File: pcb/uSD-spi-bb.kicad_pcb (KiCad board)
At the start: 2 copper layers, 36 x 36 mm, 25 parts, among them U1 TLV70233DBV, U2 MicroSD

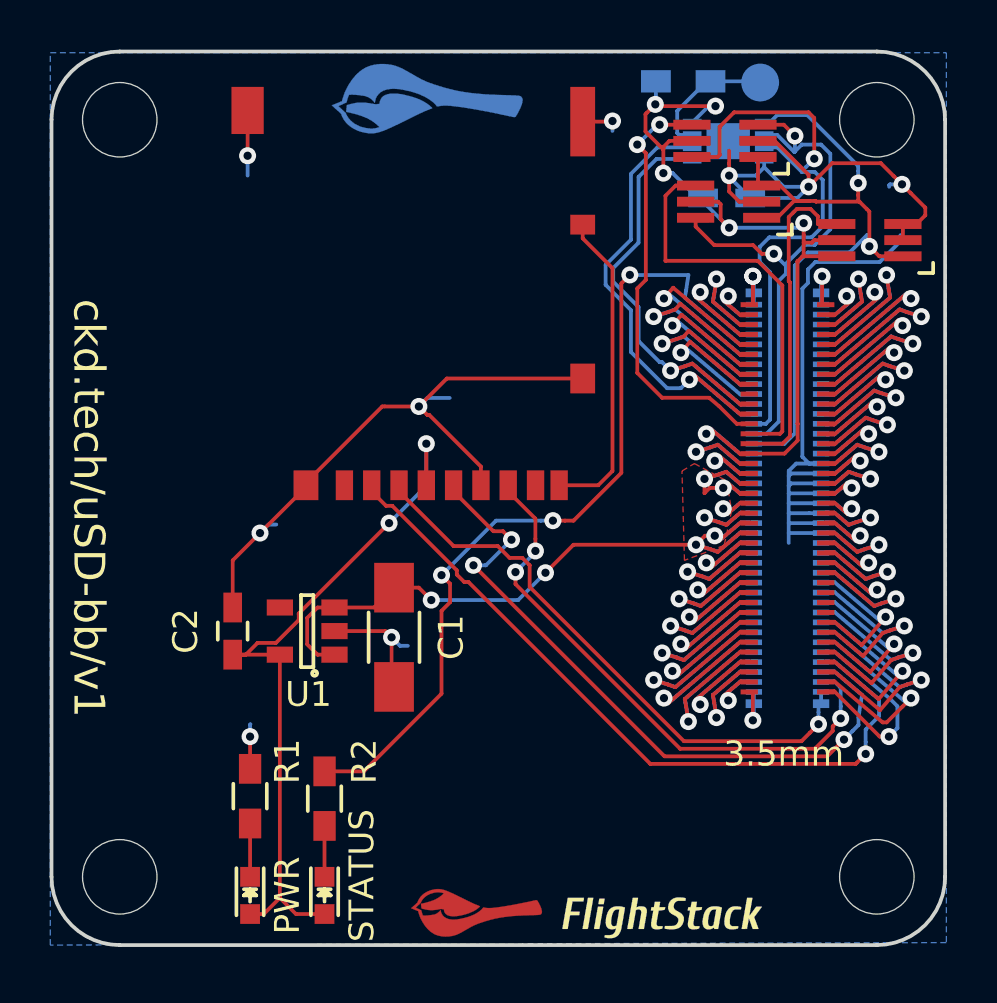
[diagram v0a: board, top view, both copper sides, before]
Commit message: Add card detect to uSD BB.
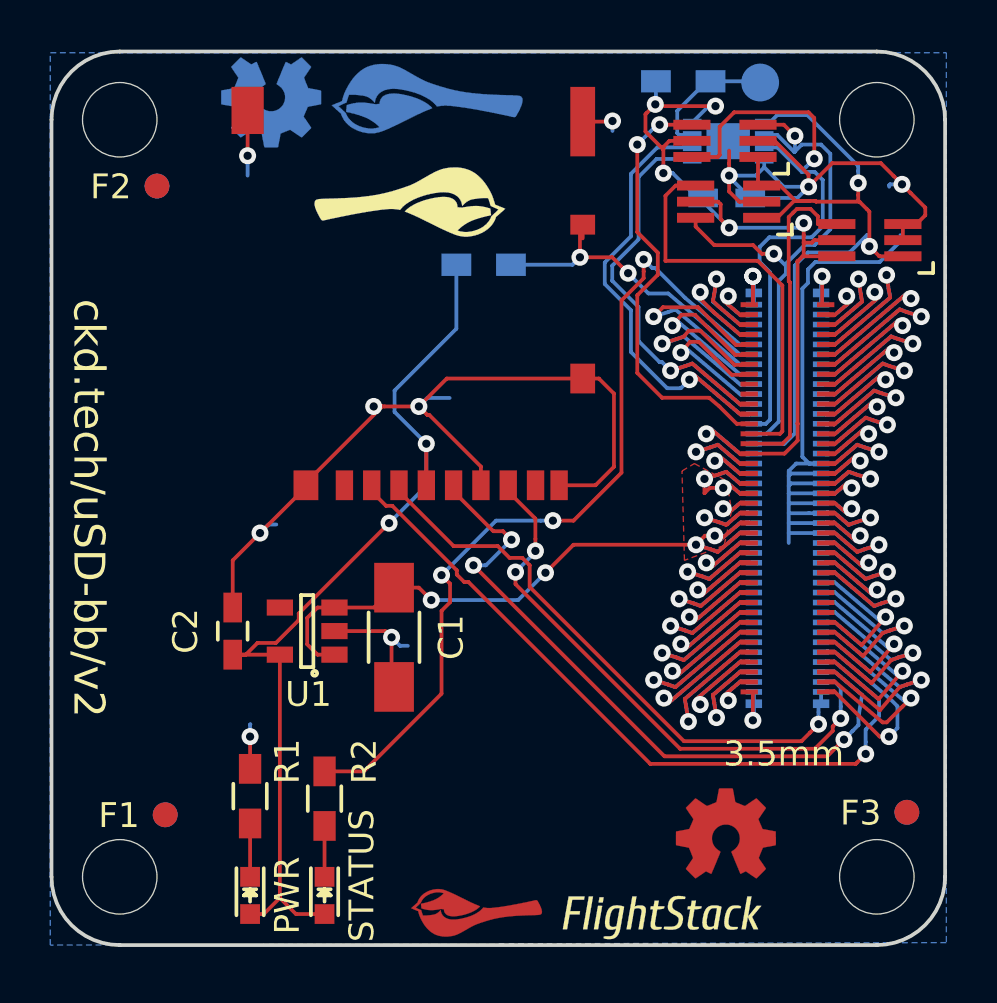
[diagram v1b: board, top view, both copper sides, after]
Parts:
- removed the G*** at (154.6, 124.9)
- removed the G*** at (131.5, 108.1)
- added F1: 1mm, macrofab:Fiducial, F.Cu at (134.6, 120.8)
- added F2: 1mm, macrofab:Fiducial, F.Cu at (134.2, 95.4)
- added F3: 1mm, macrofab:Fiducial, F.Cu at (164.5, 120.7)
- added F4: 1mm, macrofab:Fiducial, B.Cu at (134.6, 120.8)
- added F5: 1mm, macrofab:Fiducial, B.Cu at (134.2, 95.4)
- added F6: 1mm, macrofab:Fiducial, B.Cu at (164.5, 120.7)
- added G***: LOGO, flightstack:flightstack_thin-8mm, F.Cu at (154.6, 124.9)
- added G***: LOGO, flightstack:flightstack_thin-12mm, B.Cu at (131.5, 108.1)
- added G***: OSHW, oshw:oshw-4mm, B.Cu at (138.8, 92.0)
- added G***: OSHW, oshw:oshw-4mm, F.Cu at (157.2, 121.5)
- added G***: LOGO, chickadee:chickadee_3mm_ss, F.Cu at (144.3, 96.0)
- added R3: 10k, Resistors_SMD:R_0603_HandSoldering, B.Cu at (147.4, 98.6)
- U2: footprint microsd:DM3AT -> DM3AT
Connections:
- PORT_OUT1 pad 5: /ExpansionPort/GPIO2 -> /ExpansionPort/GPIO3
- PORT_OUT1 pad 6: /ExpansionPort/GPIO3 -> /ExpansionPort/GPIO4
- PORT_OUT1 pad 7: /ExpansionPort/GPIO4 -> /ExpansionPort/GPIO5
- PORT_OUT1 pad 8: /ExpansionPort/GPIO5 -> /ExpansionPort/GPIO6
- PORT_OUT1 pad 9: /ExpansionPort/GPIO6 -> Net-(PORT_OUT1-Pad9)
- U2 pad 9: Net-(U2-Pad9) -> GNDPWR
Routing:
- net Net-(U2-Pad9): track 12.8 -> 0.00 mm
- net +3V3: track 29.4 -> 38.2 mm
- net GNDPWR: track 116.0 -> 123.4 mm, vias 17 -> 18
- net /ExpansionPort/GPIO2: track 8.93 -> 13.2 mm, vias 1 -> 2
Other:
- board text added: "ckd.tech/uSD-bb/v2"
- board text removed: "ckd.tech/uSD-bb/v1"

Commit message: Rebrand everything to Polystack and increment versions.
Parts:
- removed the G*** at (154.6, 124.9)
- removed the G*** at (131.5, 108.1)
- added svg2mod: G***, polystack:polystack-medium-0.4, B.Cu at (164.9, 107.9)
- added svg2mod: G***, polystack:polystack-medium-0.4, F.Cu at (164.9, 107.9)
- added svg2mod: G***, polystack:polystack-medium-0.5, F.Cu at (154.8, 124.5)
- moved G*** 8.60 mm to (147.4, 92.2), turned to 180 degrees
- moved G*** 4.42 mm to (140.7, 92.3), turned to 180 degrees
- turned G*** to 0 degrees
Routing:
- net GNDPWR: track 123.4 -> 122.4 mm
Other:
- rule pad_to_mask_clearance: 0.2 -> 0.0762
- board text added: "ckd.tech/uSD-bb/v3"
- board text removed: "ckd.tech/uSD-bb/v2"

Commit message: Final gerbers for test manufacturing run.
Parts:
- moved U2 1.05 mm to (145.0, 99.8)
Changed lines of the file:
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@@
     (links 144)
     (no_connects 0)
-    (area 129.924999 89.924999 166.075001 126.075001)
+    (area 118.127143 74.1 234.166668 178)
     (thickness 1.6)
     (drawings 30)
@@
     (visible_elements FFFFFF7F)
     (pcbplotparams
-      (layerselection 0x010f0_80000001)
+      (layerselection 0x010fc_80000001)
       (usegerberextensions true)
       (excludeedgelayer true)
@@
     (add_net "Net-(U2-Pad1)")
     (add_net "Net-(U2-Pad8)")
+  )
+  (module DM3AT (layer F.Cu)
+    (at 145 99.75 180)
+    (fp_text reference U2 (at 0 1.55 180) (layer F.SilkS) hide
+      (effects (font (size 1 1) (thickness 0.15)))
+    )
+    (fp_text value MicroSD (at 0 0.55 360) (layer F.Fab)
+      (effects (font (size 1 1) (thickness 0.15)))
+    )
+    (fp_line (start -7.11 -4.35) (end -5.51 -4.41) (layer F.CrtYd) (width 0.15))
+    (fp_line (start -7.16 -6.66) (end -7.11 -4.35) (layer F.CrtYd) (width 0.15))
+    (fp_line (start -5.68 -6.6) (end -7.16 -6.66) (layer F.CrtYd) (width 0.15))
+    (fp_line (start -5.57 -4.53) (end -5.68 -6.6) (layer F.CrtYd) (width 0.15))
+    (fp_line (start -7.11 0.39) (end -7.05 -2.51) (layer F.CrtYd) (width 0.15))
+    (fp_line (start -5.63 0.39) (end -7.11 0.39) (layer F.CrtYd) (width 0.15))
+    (fp_line (start -5.63 -2.51) (end -5.63 0.39) (layer F.CrtYd) (width 0.15))
+    (fp_line (start -6.99 -2.51) (end -5.63 -2.51) (layer F.CrtYd) (width 0.15))
+    (fp_line (start -4.62 -0.92) (end -4.56 -2.63) (layer F.CrtYd) (width 0.15))
+    (fp_line (start 3.73 -0.86) (end -4.62 -0.92) (layer F.CrtYd) (width 0.15))
+    (fp_line (start 3.73 -2.63) (end 3.73 -0.86) (layer F.CrtYd) (width 0.15))
+    (fp_line (start -4.44 -2.63) (end 3.73 -2.63) (layer F.CrtYd) (width 0.15))
+    (fp_line (start -4.56 7.49) (end -5.57 7.55) (layer F.CrtYd) (width 0.15))
+    (fp_line (start -4.62 -0.44) (end -4.56 7.49) (layer F.CrtYd) (width 0.15))
+    (fp_line (start -5.45 -0.44) (end -4.62 -0.44) (layer F.CrtYd) (width 0.15))
+    (fp_line (start -5.51 7.55) (end -5.45 -0.44) (layer F.CrtYd) (width 0.15))
+    (fp_line (start 4.12 7.45) (end 5.5 7.45) (layer F.CrtYd) (width 0.15))
+    (fp_line (start 4.16 8.36) (end 4.12 7.45) (layer F.CrtYd) (width 0.15))
+    (fp_line (start 5.5 8.4) (end 4.16 8.36) (layer F.CrtYd) (width 0.15))
+    (fp_line (start 5.5 7.45) (end 5.5 8.4) (layer F.CrtYd) (width 0.15))
+    (fp_line (start -5.5 9.825) (end 5.5 9.825) (layer F.Fab) (width 0.15))
+    (pad 1 smd rect (at 3.2 -7.725 180) (size 0.7 1.2) (layers F.Cu F.Paste F.Mask)
+      (net 81 "Net-(U2-Pad1)"))
+    (pad 2 smd rect (at 2.1 -7.725 180) (size 0.7 1.2) (layers F.Cu F.Paste F.Mask)
+      (net 22 /ExpansionPort/SPI1_NSS))
+    (pad 3 smd rect (at 1 -7.725 180) (size 0.7 1.2) (layers F.Cu F.Paste F.Mask)
+      (net 16 /ExpansionPort/SPI1_MOSI))
+    (pad 4 smd rect (at -0.1 -7.725 180) (size 0.7 1.2) (layers F.Cu F.Paste F.Mask)
+      (net 11 +3V3))
+    (pad 5 smd rect (at -1.2 -7.725 180) (size 0.7 1.2) (layers F.Cu F.Paste F.Mask)
+      (net 21 /ExpansionPort/SPI1_SCK))
+    (pad 6 smd rect (at -2.3 -7.725 180) (size 0.7 1.2) (layers F.Cu F.Paste F.Mask)
+      (net 2 GNDPWR))
+    (pad 7 smd rect (at -3.4 -7.725 180) (size 0.7 1.2) (layers F.Cu F.Paste F.Mask)
+      (net 20 /ExpansionPort/SPI1_MISO))
+    (pad 8 smd rect (at -4.5 -7.725 180) (size 0.7 1.2) (layers F.Cu F.Paste F.Mask)
+      (net 82 "Net-(U2-Pad8)"))
+    (pad 9 smd rect (at -5.45 -7.725 180) (size 0.7 1.2) (layers F.Cu F.Paste F.Mask)
+      (net 2 GNDPWR))
+    (pad 10 smd rect (at 4.75 -7.725 180) (size 1 1.2) (layers F.Cu F.Paste F.Mask)
+      (net 2 GNDPWR))
+    (pad 11 smd rect (at 7.1 7.375 180) (size 1.3 1.9) (layers F.Cu F.Paste F.Mask)
+      (net 2 GNDPWR))
+    (pad 12 smd rect (at -6.4 6.925 180) (size 1 2.8) (layers F.Cu F.Paste F.Mask)
+      (net 2 GNDPWR))
+    (pad 14 smd rect (at -6.4 2.775 180) (size 1 0.8) (layers F.Cu F.Paste F.Mask)
+      (net 54 /ExpansionPort/GPIO2))
+    (pad 13 smd rect (at -6.4 -3.425 180) (size 1 1.2) (layers F.Cu F.Paste F.Mask)
+      (net 2 GNDPWR))
   )
   (module polystack:polystack-medium-0.4 (layer B.Cu)
@@
       (solder_mask_margin 0.5) (solder_paste_margin_ratio -0.5) (clearance 0.5))
   )
-  (module DM3AT (layer F.Cu)
-    (at 145 98.7 180)
-    (fp_text reference U2 (at 0 0.5 180) (layer F.SilkS) hide
-      (effects (font (size 1 1) (thickness 0.15)))
-    )
-    (fp_text value MicroSD (at 0 -0.5 360) (layer F.Fab)
-      (effects (font (size 1 1) (thickness 0.15)))
-    )
-    (fp_line (start -7.11 -5.4) (end -5.51 -5.46) (layer F.CrtYd) (width 0.15))
-    (fp_line (start -7.16 -7.71) (end -7.11 -5.4) (layer F.CrtYd) (width 0.15))
-    (fp_line (start -5.68 -7.65) (end -7.16 -7.71) (layer F.CrtYd) (width 0.15))
-    (fp_line (start -5.57 -5.58) (end -5.68 -7.65) (layer F.CrtYd) (width 0.15))
-    (fp_line (start -7.11 -0.66) (end -7.05 -3.56) (layer F.CrtYd) (width 0.15))
-    (fp_line (start -5.63 -0.66) (end -7.11 -0.66) (layer F.CrtYd) (width 0.15))
-    (fp_line (start -5.63 -3.56) (end -5.63 -0.66) (layer F.CrtYd) (width 0.15))
-    (fp_line (start -6.99 -3.56) (end -5.63 -3.56) (layer F.CrtYd) (width 0.15))
-    (fp_line (start -4.62 -1.97) (end -4.56 -3.68) (layer F.CrtYd) (width 0.15))
-    (fp_line (start 3.73 -1.91) (end -4.62 -1.97) (layer F.CrtYd) (width 0.15))
-    (fp_line (start 3.73 -3.68) (end 3.73 -1.91) (layer F.CrtYd) (width 0.15))
-    (fp_line (start -4.44 -3.68) (end 3.73 -3.68) (layer F.CrtYd) (width 0.15))
-    (fp_line (start -4.56 6.44) (end -5.57 6.5) (layer F.CrtYd) (width 0.15))
-    (fp_line (start -4.62 -1.49) (end -4.56 6.44) (layer F.CrtYd) (width 0.15))
-    (fp_line (start -5.45 -1.49) (end -4.62 -1.49) (layer F.CrtYd) (width 0.15))
-    (fp_line (start -5.51 6.5) (end -5.45 -1.49) (layer F.CrtYd) (width 0.15))
-    (fp_line (start 4.12 6.4) (end 5.5 6.4) (layer F.CrtYd) (width 0.15))
-    (fp_line (start 4.16 7.31) (end 4.12 6.4) (layer F.CrtYd) (width 0.15))
-    (fp_line (start 5.5 7.35) (end 4.16 7.31) (layer F.CrtYd) (width 0.15))
-    (fp_line (start 5.5 6.4) (end 5.5 7.35) (layer F.CrtYd) (width 0.15))
-    (fp_line (start -5.5 8.775) (end 5.5 8.775) (layer F.Fab) (width 0.15))
-    (pad 1 smd rect (at 3.2 -8.775 180) (size 0.7 1.2) (layers F.Cu F.Paste F.Mask)
-      (net 81 "Net-(U2-Pad1)"))
-    (pad 2 smd rect (at 2.1 -8.775 180) (size 0.7 1.2) (layers F.Cu F.Paste F.Mask)
-      (net 22 /ExpansionPort/SPI1_NSS))
-    (pad 3 smd rect (at 1 -8.775 180) (size 0.7 1.2) (layers F.Cu F.Paste F.Mask)
-      (net 16 /ExpansionPort/SPI1_MOSI))
-    (pad 4 smd rect (at -0.1 -8.775 180) (size 0.7 1.2) (layers F.Cu F.Paste F.Mask)
-      (net 11 +3V3))
-    (pad 5 smd rect (at -1.2 -8.775 180) (size 0.7 1.2) (layers F.Cu F.Paste F.Mask)
-      (net 21 /ExpansionPort/SPI1_SCK))
-    (pad 6 smd rect (at -2.3 -8.775 180) (size 0.7 1.2) (layers F.Cu F.Paste F.Mask)
-      (net 2 GNDPWR))
-    (pad 7 smd rect (at -3.4 -8.775 180) (size 0.7 1.2) (layers F.Cu F.Paste F.Mask)
-      (net 20 /ExpansionPort/SPI1_MISO))
-    (pad 8 smd rect (at -4.5 -8.775 180) (size 0.7 1.2) (layers F.Cu F.Paste F.Mask)
-      (net 82 "Net-(U2-Pad8)"))
-    (pad 9 smd rect (at -5.45 -8.775 180) (size 0.7 1.2) (layers F.Cu F.Paste F.Mask)
-      (net 2 GNDPWR))
-    (pad 10 smd rect (at 4.75 -8.775 180) (size 1 1.2) (layers F.Cu F.Paste F.Mask)
-      (net 2 GNDPWR))
-    (pad 11 smd rect (at 7.1 6.325 180) (size 1.3 1.9) (layers F.Cu F.Paste F.Mask)
-      (net 2 GNDPWR))
-    (pad 12 smd rect (at -6.4 5.875 180) (size 1 2.8) (layers F.Cu F.Paste F.Mask)
-      (net 2 GNDPWR))
-    (pad 14 smd rect (at -6.4 1.725 180) (size 1 0.8) (layers F.Cu F.Paste F.Mask)
-      (net 54 /ExpansionPort/GPIO2))
-    (pad 13 smd rect (at -6.4 -4.475 180) (size 1 1.2) (layers F.Cu F.Paste F.Mask)
-      (net 2 GNDPWR))
-  )
   (module DF40-80pin-Header (layer B.Cu)

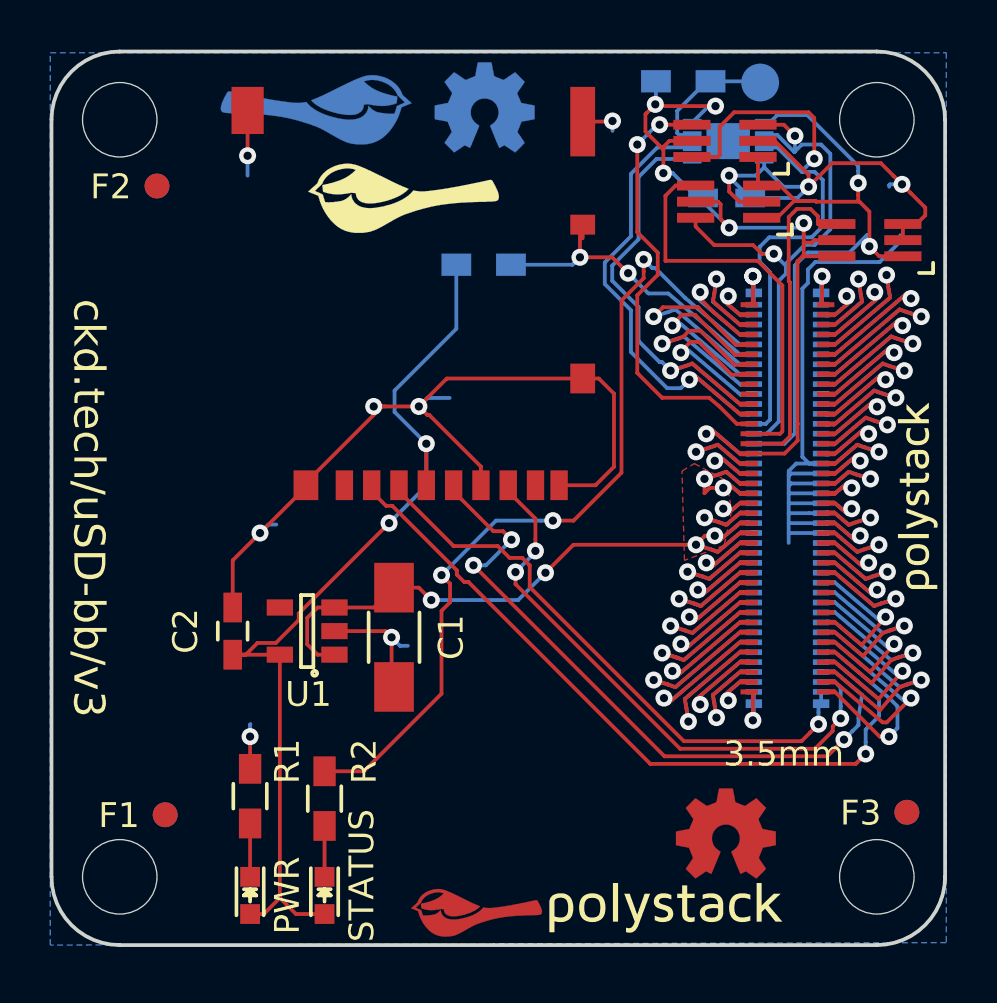
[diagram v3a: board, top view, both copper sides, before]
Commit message: Update polystack logo to bold variant, remove 'bb' from url and bump version number.
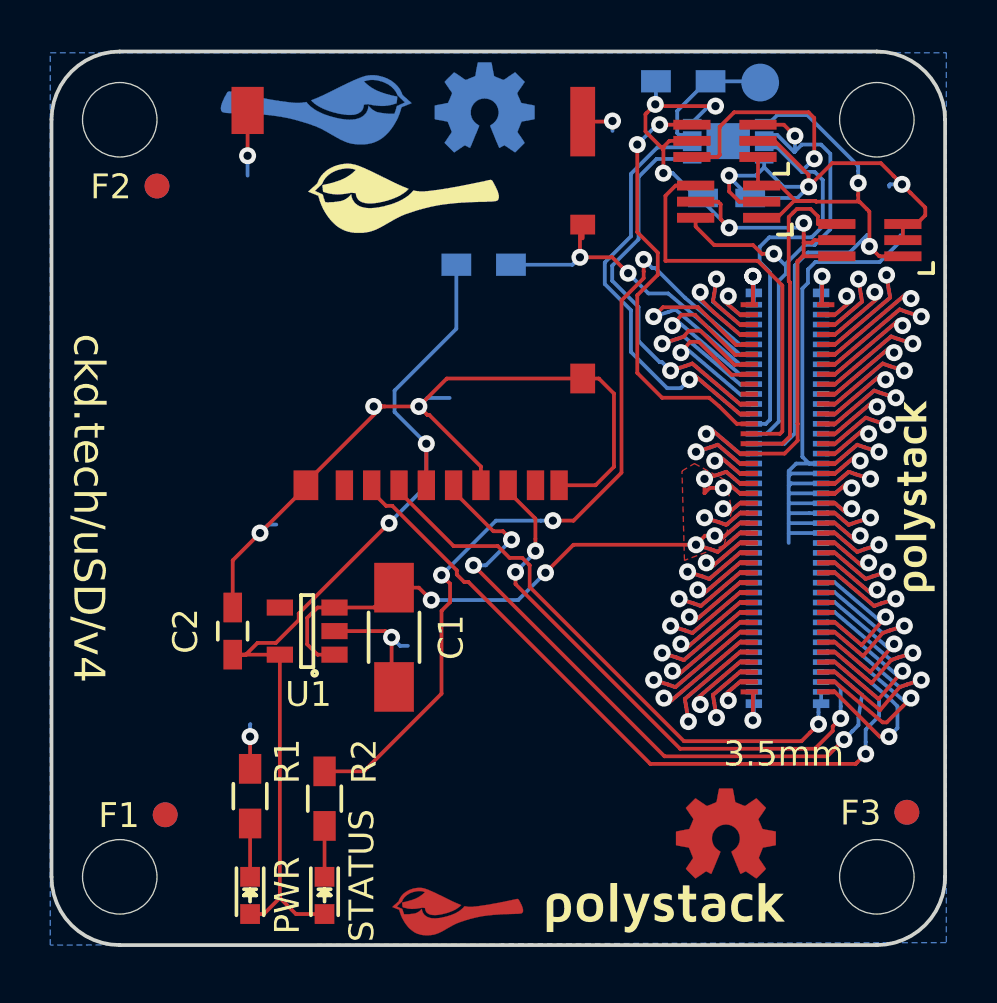
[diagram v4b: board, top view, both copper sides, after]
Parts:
- svg2mod: footprint polystack:polystack-medium-0.5 -> polystack:polystack-bold-0.5
- svg2mod (x2): footprint polystack:polystack-medium-0.4 -> polystack:polystack-bold-0.4
- moved G*** 0.76 mm to (146.3, 124.7)
- moved svg2mod 0.10 mm to (164.8, 107.9) (x2)
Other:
- board text added: "ckd.tech/uSD/v4"
- board text removed: "ckd.tech/uSD-bb/v3"

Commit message: Add license information to many files. PCB design files are CC-BY and code is MIT license.
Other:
- board text added: "Copyright 2016 Chickadee Tech LLC, <add attributions here> This work is licensed under the Creative Commons Attribution 4.0 International License. To view a copy of this license, visit http://creativecommons.org/licenses/by/4.0/ or send a letter to Creative Commons, PO Box 1866, Mountain View, CA 94042, USA."
- board text added: "Remove all Chickadee Tech LLC trademarks before making your own board. The Chickadee logo and Polystack logo are owned by Chickadee Tech LLC. You may license the Polystack logo for free by emailing support@chickadee.tech and receiving express written permission from Chickadee Tech LLC."
- board text added: "The gear logo is a mark designating open source hardware. Remove it if your design does not comply with the open source hardware definition."
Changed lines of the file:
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@@
     (links 144)
     (no_connects 0)
-    (area 118.127143 74.1 234.166668 178)
+    (area 67.58 74.1 280.690001 192.07)
     (thickness 1.6)
-    (drawings 30)
+    (drawings 38)
     (tracks 1034)
     (zones 0)
@@
     (40 Dwgs.User user)
     (41 Cmts.User user)
-    (42 Eco1.User user hide)
+    (42 Eco1.User user)
     (43 Eco2.User user)
     (44 Edge.Cuts user)
@@
       (xy 2.990233 -0.444493)) (layer B.SilkS) (width 0))
   )
+  (gr_line (start 109.67 109.14) (end 163.45 107.97) (layer Cmts.User) (width 0.2))
+  (gr_line (start 109.35 108.93) (end 143.42 123.62) (layer Cmts.User) (width 0.2))
+  (gr_line (start 139.69 94.98) (end 109.35 108.93) (layer Cmts.User) (width 0.2))
+  (gr_text "Remove all Chickadee Tech LLC trademarks\nbefore making your own board. The\nChickadee logo and Polystack logo\nare owned by Chickadee Tech LLC.\n\nYou may license the Polystack logo for\nfree by emailing support@chickadee.tech\nand receiving express written permission\nfrom Chickadee Tech LLC." (at 67.73 110.52) (layer Cmts.User)
+    (effects (font (size 1.5 1.5) (thickness 0.3)) (justify left))
+  )
+  (gr_line (start 176.23 115.42) (end 149.97 93.54) (layer Cmts.User) (width 0.2))
+  (gr_line (start 159.3 120.83) (end 176.23 115.42) (layer Cmts.User) (width 0.2))
+  (gr_text "The gear logo is a mark designating open\nsource hardware. Remove it if your design\ndoes not comply with the open source\nhardware definition." (at 176.8 115.42) (layer Cmts.User)
+    (effects (font (size 1.5 1.5) (thickness 0.3)) (justify left))
+  )
+  (gr_text "Copyright 2016 Chickadee Tech LLC, <add attributions here>\n\nThis work is licensed under the Creative Commons Attribution 4.0 International License.\nTo view a copy of this license, visit http://creativecommons.org/licenses/by/4.0/\nor send a letter to Creative Commons, PO Box 1866, Mountain View, CA 94042, USA." (at 179.04 173.93) (layer Cmts.User)
+    (effects (font (size 1.5 1.5) (thickness 0.3)) (justify left))
+  )
   (gr_text ckd.tech/uSD/v4 (at 131.5 108.4 270) (layer F.SilkS)
     (effects (font (size 1.25 1.25) (thickness 0.2)))
@@
     (effects (font (size 1.5 1.5) (thickness 0.3)))
   )
-  (gr_text Front (at 121.17 108.99) (layer Cmts.User)
+  (gr_text Front (at 126.08 111.27) (layer Cmts.User)
     (effects (font (size 1.5 1.5) (thickness 0.3)))
   )
@@
   (gr_line (start 166 92.75) (end 166 123.25) (angle 90) (layer Edge.Cuts) (width 0.15))
   (gr_line (start 132.75 90) (end 163.25 90) (angle 90) (layer Edge.Cuts) (width 0.15))
-  (gr_text uSD-spi-bb (at 187.25 174.25) (layer Cmts.User)
-    (effects (font (size 5 5) (thickness 0.5)) (justify left))
+  (gr_text uSD-spi-bb (at 187.39 189.72) (layer Cmts.User)
+    (effects (font (size 3 3) (thickness 0.5)) (justify left))
   )
   (segment (start 162.95 97.849974) (end 162.95 96.45) (width 0.1524) (layer F.Cu) (net 1))
